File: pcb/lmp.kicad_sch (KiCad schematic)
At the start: 8 parts, among them J4 TB0011-350-03GR, J5 0528070310, J6 Conn_01x03_Pin, U5 LMP91000SDX/NOPB

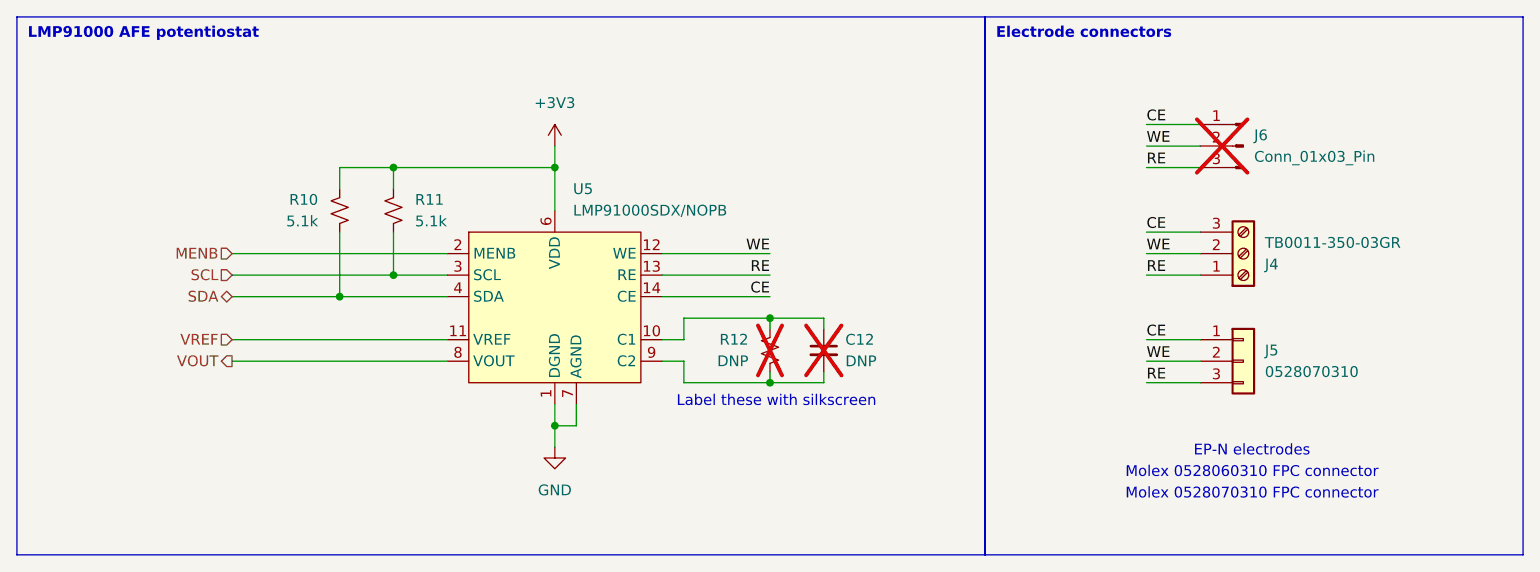
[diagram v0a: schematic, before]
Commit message: add c1 and int1 to pcb
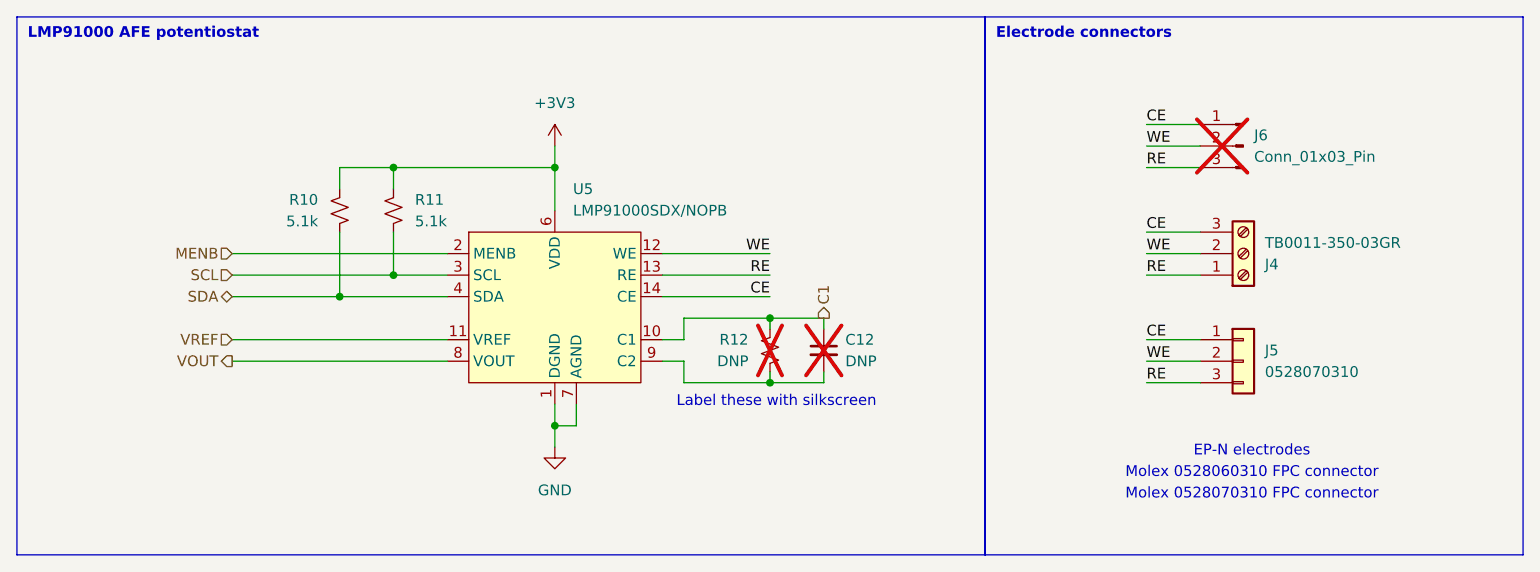
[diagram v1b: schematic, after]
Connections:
- net C1: now reaches C12.1, R12.1, U5.10 (C1)
